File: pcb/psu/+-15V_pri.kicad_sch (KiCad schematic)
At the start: 15 parts, among them J2 Conn_01x03_Socket, U1 LTC3260xDE

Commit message: poprawki do schematu psu
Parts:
- renumbered C5 to C10, C7 to C4, C4 to C5, C3 to C6, C1 to C7, C2 to C8, C6 to C9, R1 to R2, R2 to R5, TP6 to TP4, U1 to U3
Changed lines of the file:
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@@
 		(dnp no)
 		(fields_autoplaced yes)
-		(property "Reference" "TP6"
+		(property "Reference" "TP4"
 			(at 200.66 97.0279 0)
 			(effects
@@
 			(project "Nanopozycjoner_Power_Supply"
 				(path "/41f68583-7750-4b74-a26b-68c1e6d5dd9b/ba82f417-cd94-4294-a988-f461f1e7f3c2"
-					(reference "TP6")
+					(reference "TP4")
 					(unit 1)
 				)
@@
 		(dnp no)
 		(fields_autoplaced yes)
-		(property "Reference" "R2"
+		(property "Reference" "R5"
 			(at 152.4 119.3799 0)
 			(effects
@@
 			(project "Nanopozycjoner_Power_Supply"
 				(path "/41f68583-7750-4b74-a26b-68c1e6d5dd9b/ba82f417-cd94-4294-a988-f461f1e7f3c2"
-					(reference "R2")
+					(reference "R5")
 					(unit 1)
 				)
@@
 		(on_board yes)
 		(dnp no)
-		(property "Reference" "C2"
+		(property "Reference" "C8"
 			(at 139.7 106.6799 0)
 			(effects
@@
 			(project "Nanopozycjoner_Power_Supply"
 				(path "/41f68583-7750-4b74-a26b-68c1e6d5dd9b/ba82f417-cd94-4294-a988-f461f1e7f3c2"
-					(reference "C2")
+					(reference "C8")
 					(unit 1)
 				)
@@
 		(on_board yes)
 		(dnp no)
-		(property "Reference" "C7"
+		(property "Reference" "C4"
 			(at 101.854 87.376 0)
 			(effects
@@
 			(project "Nanopozycjoner_Power_Supply"
 				(path "/41f68583-7750-4b74-a26b-68c1e6d5dd9b/ba82f417-cd94-4294-a988-f461f1e7f3c2"
-					(reference "C7")
+					(reference "C4")
 					(unit 1)
 				)
@@
 		(dnp no)
 		(fields_autoplaced yes)
-		(property "Reference" "#PWR05"
+		(property "Reference" "#PWR09"
 			(at 105.41 97.79 0)
 			(effects
@@
 			(project "Nanopozycjoner_Power_Supply"
 				(path "/41f68583-7750-4b74-a26b-68c1e6d5dd9b/ba82f417-cd94-4294-a988-f461f1e7f3c2"
-					(reference "#PWR05")
+					(reference "#PWR09")
 					(unit 1)
 				)
@@
 		(dnp no)
 		(fields_autoplaced yes)
-		(property "Reference" "#PWR018"
+		(property "Reference" "#PWR016"
 			(at 204.47 120.65 0)
 			(effects
@@
 			(project "Nanopozycjoner_Power_Supply"
 				(path "/41f68583-7750-4b74-a26b-68c1e6d5dd9b/ba82f417-cd94-4294-a988-f461f1e7f3c2"
-					(reference "#PWR018")
+					(reference "#PWR016")
 					(unit 1)
 				)
@@
 		(on_board yes)
 		(dnp no)
-		(property "Reference" "C3"
+		(property "Reference" "C6"
 			(at 107.95 119.3799 0)
 			(effects
@@
 			(project "Nanopozycjoner_Power_Supply"
 				(path "/41f68583-7750-4b74-a26b-68c1e6d5dd9b/ba82f417-cd94-4294-a988-f461f1e7f3c2"
-					(reference "C3")
+					(reference "C6")
 					(unit 1)
 				)
@@
 		(dnp no)
 		(fields_autoplaced yes)
-		(property "Reference" "#PWR01"
+		(property "Reference" "#PWR010"
 			(at 105.41 118.11 0)
 			(effects
@@
 			(project ""
 				(path "/41f68583-7750-4b74-a26b-68c1e6d5dd9b/ba82f417-cd94-4294-a988-f461f1e7f3c2"
-					(reference "#PWR01")
+					(reference "#PWR010")
 					(unit 1)
 				)
@@
 		(dnp no)
 		(fields_autoplaced yes)
-		(property "Reference" "#PWR04"
+		(property "Reference" "#PWR013"
 			(at 168.91 127 0)
 			(effects
@@
 			(project "Nanopozycjoner_Power_Supply"
 				(path "/41f68583-7750-4b74-a26b-68c1e6d5dd9b/ba82f417-cd94-4294-a988-f461f1e7f3c2"
-					(reference "#PWR04")
+					(reference "#PWR013")
 					(unit 1)
 				)
@@
 		(dnp no)
 		(fields_autoplaced yes)
-		(property "Reference" "#PWR02"
+		(property "Reference" "#PWR012"
 			(at 168.91 110.49 0)
 			(effects
@@
 			(project "Nanopozycjoner_Power_Supply"
 				(path "/41f68583-7750-4b74-a26b-68c1e6d5dd9b/ba82f417-cd94-4294-a988-f461f1e7f3c2"
-					(reference "#PWR02")
+					(reference "#PWR012")
 					(unit 1)
 				)
@@
 		(dnp no)
 		(fields_autoplaced yes)
-		(property "Reference" "U1"
+		(property "Reference" "U3"
 			(at 125.73 72.39 0)
 			(effects
@@
 			(project ""
 				(path "/41f68583-7750-4b74-a26b-68c1e6d5dd9b/ba82f417-cd94-4294-a988-f461f1e7f3c2"
-					(reference "U1")
+					(reference "U3")
 					(unit 1)
 				)
@@
 		(dnp no)
 		(fields_autoplaced yes)
-		(property "Reference" "#PWR017"
+		(property "Reference" "#PWR015"
 			(at 204.47 109.22 0)
 			(effects
@@
 			(project "Nanopozycjoner_Power_Supply"
 				(path "/41f68583-7750-4b74-a26b-68c1e6d5dd9b/ba82f417-cd94-4294-a988-f461f1e7f3c2"
-					(reference "#PWR017")
+					(reference "#PWR015")
 					(unit 1)
 				)
@@
 		(on_board yes)
 		(dnp no)
-		(property "Reference" "C4"
+		(property "Reference" "C5"
 			(at 107.442 107.188 90)
 			(effects
@@
 			(project "Nanopozycjoner_Power_Supply"
 				(path "/41f68583-7750-4b74-a26b-68c1e6d5dd9b/ba82f417-cd94-4294-a988-f461f1e7f3c2"
-					(reference "C4")
+					(reference "C5")
 					(unit 1)
 				)
@@
 		(dnp no)
 		(fields_autoplaced yes)
-		(property "Reference" "R1"
+		(property "Reference" "R2"
 			(at 152.4 83.8199 0)
 			(effects
@@
 			(project ""
 				(path "/41f68583-7750-4b74-a26b-68c1e6d5dd9b/ba82f417-cd94-4294-a988-f461f1e7f3c2"
-					(reference "R1")
+					(reference "R2")
 					(unit 1)
 				)
@@
 		(on_board yes)
 		(dnp no)
-		(property "Reference" "C1"
+		(property "Reference" "C7"
 			(at 139.7 96.5199 0)
 			(effects
@@
 			(project ""
 				(path "/41f68583-7750-4b74-a26b-68c1e6d5dd9b/ba82f417-cd94-4294-a988-f461f1e7f3c2"
-					(reference "C1")
+					(reference "C7")
 					(unit 1)
 				)
@@
 		(on_board yes)
 		(dnp no)
-		(property "Reference" "C6"
+		(property "Reference" "C9"
 			(at 157.734 92.456 0)
 			(effects
@@
 			(project "Nanopozycjoner_Power_Supply"
 				(path "/41f68583-7750-4b74-a26b-68c1e6d5dd9b/ba82f417-cd94-4294-a988-f461f1e7f3c2"
-					(reference "C6")
+					(reference "C9")
 					(unit 1)
 				)
@@
 		(dnp no)
 		(fields_autoplaced yes)
-		(property "Reference" "#PWR019"
+		(property "Reference" "#PWR014"
 			(at 204.47 100.33 0)
 			(effects
@@
 			(project "Nanopozycjoner_Power_Supply"
 				(path "/41f68583-7750-4b74-a26b-68c1e6d5dd9b/ba82f417-cd94-4294-a988-f461f1e7f3c2"
-					(reference "#PWR019")
+					(reference "#PWR014")
 					(unit 1)
 				)
@@
 		(dnp no)
 		(fields_autoplaced yes)
-		(property "Reference" "#PWR06"
+		(property "Reference" "#PWR08"
 			(at 105.41 80.01 0)
 			(effects
@@
 			(project ""
 				(path "/41f68583-7750-4b74-a26b-68c1e6d5dd9b/ba82f417-cd94-4294-a988-f461f1e7f3c2"
-					(reference "#PWR06")
+					(reference "#PWR08")
 					(unit 1)
 				)
@@
 		(on_board yes)
 		(dnp no)
-		(property "Reference" "C5"
+		(property "Reference" "C10"
 			(at 157.734 115.316 0)
 			(effects
@@
 			(project "Nanopozycjoner_Power_Supply"
 				(path "/41f68583-7750-4b74-a26b-68c1e6d5dd9b/ba82f417-cd94-4294-a988-f461f1e7f3c2"
-					(reference "C5")
+					(reference "C10")
 					(unit 1)
 				)
@@
 		(dnp no)
 		(fields_autoplaced yes)
-		(property "Reference" "#PWR03"
+		(property "Reference" "#PWR011"
 			(at 168.91 80.01 0)
 			(effects
@@
 			(project ""
 				(path "/41f68583-7750-4b74-a26b-68c1e6d5dd9b/ba82f417-cd94-4294-a988-f461f1e7f3c2"
-					(reference "#PWR03")
-					(unit 1)
-				)
+					(reference "#PWR011")
+					(unit 1)
+				)

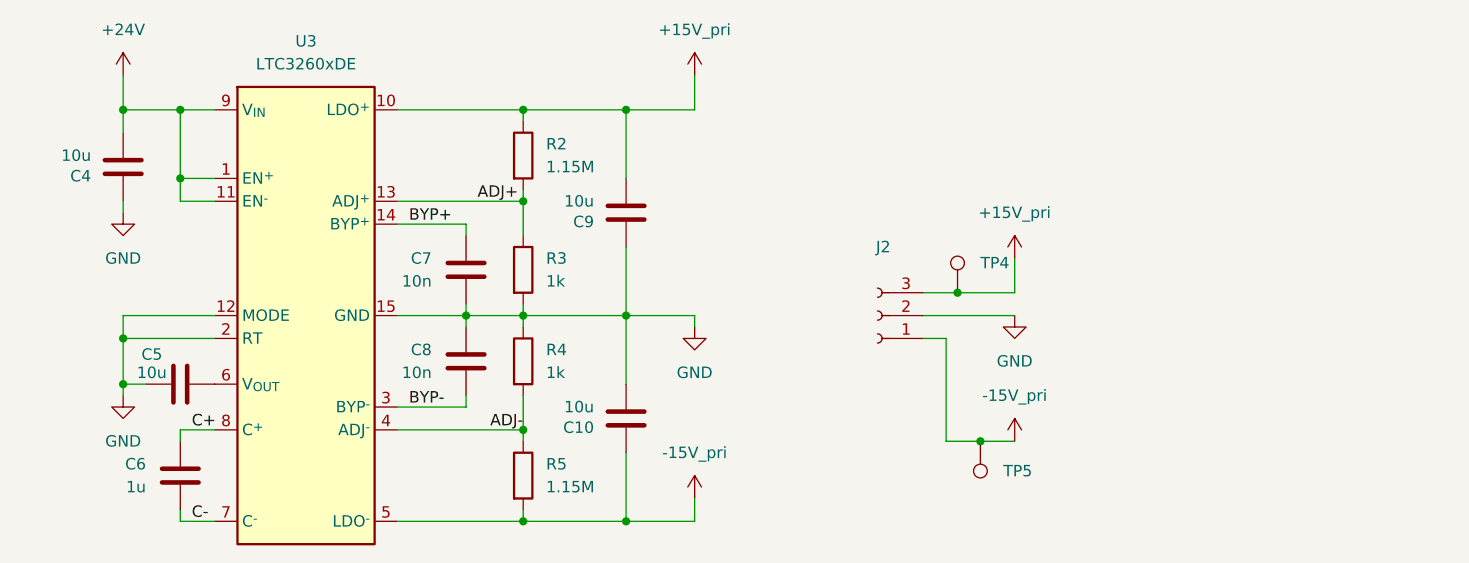
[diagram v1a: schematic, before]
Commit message: added PSU PCB design files
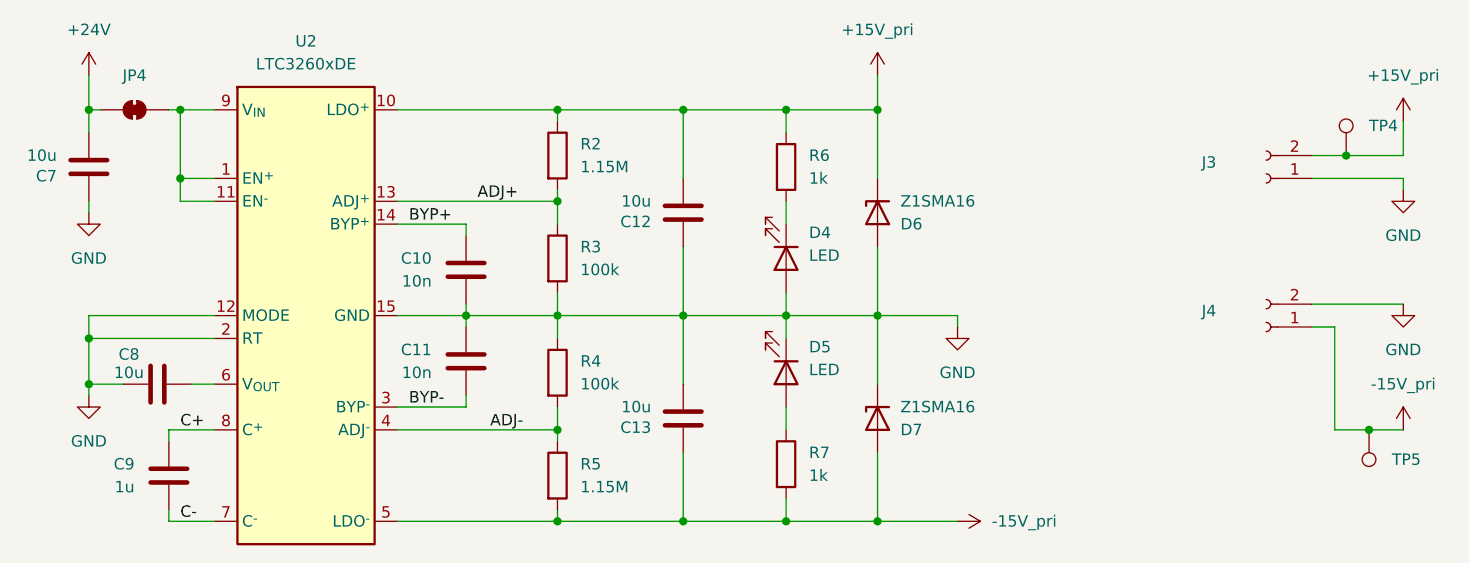
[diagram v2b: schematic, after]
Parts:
- removed J2: Conn_01x03_Socket, symbol Connector:Conn_01x03_Socket
- added D4, D5: LED, LED_SMD:LED_0603_1608Metric, symbol Device:LED
- added D6, D7: Z1SMA16, Diode_SMD:D_SMA, symbol Diode:Z1SMAxxx
- added J3, J4: Conn_01x02_Socket, Connector_Wago:Wago_734-132_1x02_P3.50mm_Vertical, symbol Connector:Conn_01x02_Socket
- added JP4: SolderJumper_2_Bridged, Jumper:SolderJumper-2_P1.3mm_Bridged2Bar_RoundedPad1.0x1.5mm, symbol Jumper:SolderJumper_2_Bridged
- added R6, R7: 1k, Resistor_SMD:R_0805_2012Metric, symbol Device:R
- C10: renamed from C7; footprint (none) -> Capacitor_SMD:C_0805_2012Metric
- C11: renamed from C8; footprint (none) -> Capacitor_SMD:C_0805_2012Metric
- C12: renamed from C9; footprint (none) -> Capacitor_SMD:C_0805_2012Metric
- C13: renamed from C10; footprint (none) -> Capacitor_SMD:C_0805_2012Metric
- C7: renamed from C4; footprint (none) -> Capacitor_SMD:C_0805_2012Metric
- C8: renamed from C5; footprint (none) -> Capacitor_SMD:C_0805_2012Metric
- C9: renamed from C6; footprint (none) -> Capacitor_SMD:C_0805_2012Metric
- R2, R5: footprint (none) -> Resistor_SMD:R_0805_2012Metric
- R3, R4: value 1k -> 100k; footprint (none) -> Resistor_SMD:R_0805_2012Metric
- TP4, TP5: footprint (none) -> TestPoint:TestPoint_Pad_D1.5mm
- renumbered U3 to U2
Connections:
- net +15V_pri: now also D6.1 (K), J3.2 (Pin_2), R6.1
- net +24V: now also JP4.1 (A); no longer U2.1 (EN^{+}), U2.11 (EN^{-}), U2.9 (V_{IN})
- net -15V_pri: now also D7.2 (A), J4.1 (Pin_1), R7.2
- net GND: now also D4.2 (A), D5.1 (K), D6.2 (A), D7.1 (K), J3.1 (Pin_1), J4.2 (Pin_2)
- new net: D4.1 (K), R6.2
- new net: D5.2 (A), R7.1
- new net: JP4.2 (B), U2.1 (EN^{+}), U2.11 (EN^{-}), U2.9 (V_{IN})
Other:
- moved on the sheet: C12, C13, C7, C8, C9, R2, R3, R4, R5, TP4, TP5

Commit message: final changes
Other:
- moved on the sheet: J3, J4, TP4, TP5
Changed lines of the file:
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@@
 	)
 	(junction
-		(at 241.3 85.09)
+		(at 233.68 86.36)
 		(diameter 0)
 		(color 0 0 0 0)
@@
 	)
 	(junction
-		(at 243.84 115.57)
+		(at 236.22 116.84)
 		(diameter 0)
 		(color 0 0 0 0)
@@
 	(wire
 		(pts
-			(xy 237.49 85.09) (xy 241.3 85.09)
+			(xy 229.87 86.36) (xy 233.68 86.36)
 		)
 		(stroke
@@
 	(wire
 		(pts
-			(xy 243.84 115.57) (xy 240.03 115.57)
+			(xy 236.22 116.84) (xy 232.41 116.84)
 		)
 		(stroke
@@
 	(wire
 		(pts
-			(xy 247.65 87.63) (xy 247.65 88.9)
+			(xy 240.03 88.9) (xy 240.03 90.17)
 		)
 		(stroke
@@
 	(wire
 		(pts
-			(xy 237.49 87.63) (xy 247.65 87.63)
+			(xy 229.87 88.9) (xy 240.03 88.9)
 		)
 		(stroke
@@
 	(wire
 		(pts
-			(xy 247.65 115.57) (xy 243.84 115.57)
+			(xy 240.03 116.84) (xy 236.22 116.84)
 		)
 		(stroke
@@
 	(wire
 		(pts
-			(xy 237.49 104.14) (xy 240.03 104.14)
+			(xy 229.87 105.41) (xy 232.41 105.41)
 		)
 		(stroke
@@
 	(wire
 		(pts
-			(xy 240.03 115.57) (xy 240.03 104.14)
+			(xy 232.41 116.84) (xy 232.41 105.41)
 		)
 		(stroke
@@
 	(wire
 		(pts
-			(xy 241.3 85.09) (xy 247.65 85.09)
+			(xy 233.68 86.36) (xy 240.03 86.36)
 		)
 		(stroke
@@
 	(wire
 		(pts
-			(xy 247.65 85.09) (xy 247.65 81.28)
+			(xy 240.03 86.36) (xy 240.03 82.55)
 		)
 		(stroke
@@
 	(wire
 		(pts
-			(xy 237.49 101.6) (xy 247.65 101.6)
+			(xy 229.87 102.87) (xy 240.03 102.87)
 		)
 		(stroke
@@
 	(symbol
 		(lib_id "power:GND")
-		(at 247.65 88.9 0)
+		(at 240.03 90.17 0)
 		(unit 1)
 		(exclude_from_sim no)
@@
 		(fields_autoplaced yes)
 		(property "Reference" "#PWR020"
-			(at 247.65 95.25 0)
+			(at 240.03 96.52 0)
 			(effects
 				(font
@@
 		)
 		(property "Value" "GND"
-			(at 247.65 93.98 0)
+			(at 240.03 95.25 0)
 			(effects
 				(font
@@
 		)
 		(property "Footprint" ""
-			(at 247.65 88.9 0)
+			(at 240.03 90.17 0)
 			(effects
 				(font
@@
 		)
 		(property "Datasheet" ""
-			(at 247.65 88.9 0)
+			(at 240.03 90.17 0)
 			(effects
 				(font
@@
 		)
 		(property "Description" "Power symbol creates a global label with name \"GND\" , ground"
-			(at 247.65 88.9 0)
+			(at 240.03 90.17 0)
 			(effects
 				(font
@@
 	(symbol
 		(lib_id "Connector:TestPoint")
-		(at 241.3 85.09 0)
+		(at 233.68 86.36 0)
 		(unit 1)
 		(exclude_from_sim no)
@@
 		(fields_autoplaced yes)
 		(property "Reference" "TP4"
-			(at 243.84 81.7879 0)
+			(at 236.22 83.0579 0)
 			(effects
 				(font
@@
 		)
 		(property "Value" "TestPoint"
-			(at 243.84 83.0579 0)
+			(at 236.22 84.3279 0)
 			(effects
 				(font
@@
 		)
 		(property "Footprint" "TestPoint:TestPoint_Pad_D1.5mm"
-			(at 246.38 85.09 0)
+			(at 238.76 86.36 0)
 			(effects
 				(font
@@
 		)
 		(property "Datasheet" "~"
-			(at 246.38 85.09 0)
+			(at 238.76 86.36 0)
 			(effects
 				(font
@@
 		)
 		(property "Description" "test point"
-			(at 241.3 85.09 0)
+			(at 233.68 86.36 0)
 			(effects
 				(font
@@
 	(symbol
 		(lib_id "power:+15V")
-		(at 247.65 115.57 0)
+		(at 240.03 116.84 0)
 		(unit 1)
 		(exclude_from_sim no)
@@
 		(fields_autoplaced yes)
 		(property "Reference" "#PWR022"
-			(at 247.65 119.38 0)
+			(at 240.03 120.65 0)
 			(effects
 				(font
@@
 		)
 		(property "Value" "-15V_pri"
-			(at 247.65 110.49 0)
+			(at 240.03 111.76 0)
 			(effects
 				(font
@@
 		)
 		(property "Footprint" ""
-			(at 247.65 115.57 0)
+			(at 240.03 116.84 0)
 			(effects
 				(font
@@
 		)
 		(property "Datasheet" ""
-			(at 247.65 115.57 0)
+			(at 240.03 116.84 0)
 			(effects
 				(font
@@
 		)
 		(property "Description" "Power symbol creates a global label with name \"+15V\""
-			(at 247.65 115.57 0)
+			(at 240.03 116.84 0)
 			(effects
 				(font
@@
 	(symbol
 		(lib_id "Connector:Conn_01x02_Socket")
-		(at 232.41 87.63 180)
+		(at 224.79 88.9 180)
 		(unit 1)
 		(exclude_from_sim no)
@@
 		(dnp no)
 		(property "Reference" "J3"
-			(at 226.06 85.852 0)
+			(at 218.44 87.122 0)
 			(effects
 				(font
@@
 		)
 		(property "Value" "Conn_01x02_Socket"
-			(at 227.838 81.788 0)
+			(at 220.218 83.058 0)
 			(effects
 				(font
@@
 		)
 		(property "Footprint" "Connector_Wago:Wago_734-132_1x02_P3.50mm_Vertical"
-			(at 232.41 87.63 0)
+			(at 224.79 88.9 0)
 			(effects
 				(font
@@
 		)
 		(property "Datasheet" "~"
-			(at 232.41 87.63 0)
+			(at 224.79 88.9 0)
 			(effects
 				(font
@@
 		)
 		(property "Description" "Generic connector, single row, 01x02, script generated"
-			(at 232.41 87.63 0)
+			(at 224.79 88.9 0)
 			(effects
 				(font
@@
 	(symbol
 		(lib_id "power:GND")
-		(at 247.65 101.6 0)
+		(at 240.03 102.87 0)
 		(unit 1)
 		(exclude_from_sim no)
@@
 		(fields_autoplaced yes)
 		(property "Reference" "#PWR021"
-			(at 247.65 107.95 0)
+			(at 240.03 109.22 0)
 			(effects
 				(font
@@
 		)
 		(property "Value" "GND"
-			(at 247.65 106.68 0)
+			(at 240.03 107.95 0)
 			(effects
 				(font
@@
 		)
 		(property "Footprint" ""
-			(at 247.65 101.6 0)
+			(at 240.03 102.87 0)
 			(effects
 				(font
@@
 		)
 		(property "Datasheet" ""
-			(at 247.65 101.6 0)
+			(at 240.03 102.87 0)
 			(effects
 				(font
@@
 		)
 		(property "Description" "Power symbol creates a global label with name \"GND\" , ground"
-			(at 247.65 101.6 0)
+			(at 240.03 102.87 0)
 			(effects
 				(font
@@
 	(symbol
 		(lib_id "power:+15V")
-		(at 247.65 81.28 0)
+		(at 240.03 82.55 0)
 		(unit 1)
 		(exclude_from_sim no)
@@
 		(fields_autoplaced yes)
 		(property "Reference" "#PWR019"
-			(at 247.65 85.09 0)
+			(at 240.03 86.36 0)
 			(effects
 				(font
@@
 		)
 		(property "Value" "+15V_pri"
-			(at 247.65 76.2 0)
+			(at 240.03 77.47 0)
 			(effects
 				(font
@@
 		)
 		(property "Footprint" ""
-			(at 247.65 81.28 0)
+			(at 240.03 82.55 0)
 			(effects
 				(font
@@
 		)
 		(property "Datasheet" ""
-			(at 247.65 81.28 0)
+			(at 240.03 82.55 0)
 			(effects
 				(font
@@
 		)
 		(property "Description" "Power symbol creates a global label with name \"+15V\""
-			(at 247.65 81.28 0)
+			(at 240.03 82.55 0)
 			(effects
 				(font
@@
 	(symbol
 		(lib_id "Connector:TestPoint")
-		(at 243.84 115.57 180)
+		(at 236.22 116.84 180)
 		(unit 1)
 		(exclude_from_sim no)
@@
 		(fields_autoplaced yes)
 		(property "Reference" "TP5"
-			(at 246.38 118.8719 0)
+			(at 238.76 120.1419 0)
 			(effects
 				(font
@@
 		)
 		(property "Value" "TestPoint"
-			(at 241.3 117.6021 0)
+			(at 233.68 118.8721 0)
 			(effects
 				(font
@@
 		)
 		(property "Footprint" "TestPoint:TestPoint_Pad_D1.5mm"
-			(at 238.76 115.57 0)
+			(at 231.14 116.84 0)
 			(effects
 				(font
@@
 		)
 		(property "Datasheet" "~"
-			(at 238.76 115.57 0)
+			(at 231.14 116.84 0)
 			(effects
 				(font
@@
 		)
 		(property "Description" "test point"
-			(at 243.84 115.57 0)
+			(at 236.22 116.84 0)
 			(effects
 				(font
@@
 	(symbol
 		(lib_id "Connector:Conn_01x02_Socket")
-		(at 232.41 104.14 180)
+		(at 224.79 105.41 180)
 		(unit 1)
 		(exclude_from_sim no)
@@
 		(dnp no)
 		(property "Reference" "J4"
-			(at 226.06 102.362 0)
+			(at 218.44 103.632 0)
 			(effects
 				(font
@@
 		)
 		(property "Value" "Conn_01x02_Socket"
-			(at 227.838 98.298 0)
+			(at 220.218 99.568 0)
 			(effects
 				(font
@@
 		)
 		(property "Footprint" "Connector_Wago:Wago_734-132_1x02_P3.50mm_Vertical"
-			(at 232.41 104.14 0)
+			(at 224.79 105.41 0)
 			(effects
 				(font
@@
 		)
 		(property "Datasheet" "~"
-			(at 232.41 104.14 0)
+			(at 224.79 105.41 0)
 			(effects
 				(font
@@
 		)
 		(property "Description" "Generic connector, single row, 01x02, script generated"
-			(at 232.41 104.14 0)
+			(at 224.79 105.41 0)
 			(effects
 				(font
